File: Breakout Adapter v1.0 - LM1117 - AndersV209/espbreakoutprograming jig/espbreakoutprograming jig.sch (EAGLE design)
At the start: 15 parts, among them X1 MINI-USB_SHIELD4P-85-32004-00X

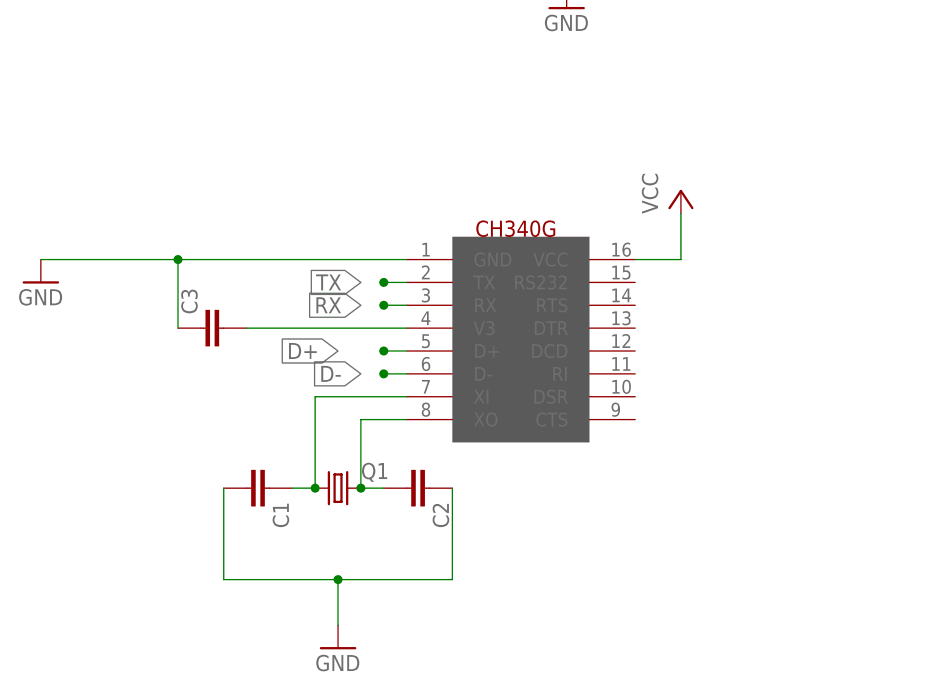
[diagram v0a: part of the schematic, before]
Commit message: update to programming jig
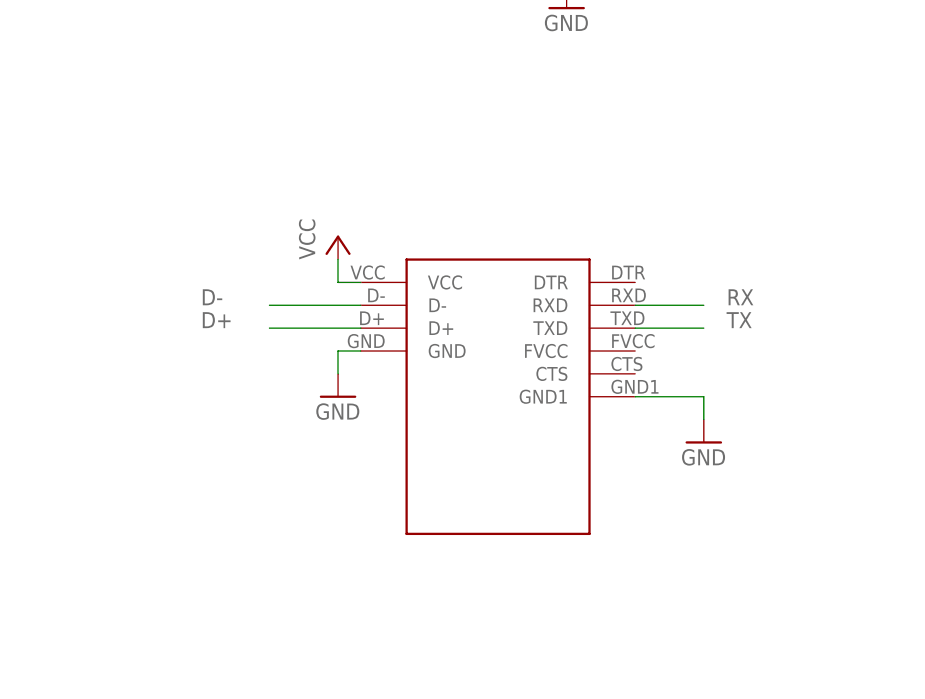
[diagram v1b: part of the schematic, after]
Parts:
- removed C1, C2, C3: (no value), rcl:C-EUC0805K
- removed Q1: (no value), adafruit:CRYSTALHC49U-V
- U$1: value CH340G -> USB-TTL; device usb-serial:CH340G -> mylib:USB-TTL
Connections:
- removed net N$1: C1.1, Q1.1, U$1.XI
- removed net N$2: C2.2, Q1.2, U$1.XO
- removed net N$3: C3.2, U$1.V3
- net GND: now also U$1.GND1; no longer C1.2, C2.1, C3.1
- net RX: now also U$1.RXD; no longer U$1.RX
- net TX: now also U$1.TXD; no longer U$1.TX
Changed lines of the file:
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@@
 </classes>
 <parts>
-<part name="U$1" library="usb-serial" deviceset="CH340G" device=""/>
 <part name="X1" library="con-cypressindustries" deviceset="MINI-USB_SHIELD4P-" device="85-32004-00X"/>
 <part name="U$2" library="mylib" deviceset="ESP12EBREAKOUT" device=""/>
@@
 <part name="P+3" library="supply1" deviceset="VCC" device=""/>
 <part name="POWER" library="mylib" deviceset="TOGGLE_SWITCH" device=""/>
-<part name="C1" library="rcl" deviceset="C-EU" device="C0805K"/>
-<part name="C2" library="rcl" deviceset="C-EU" device="C0805K"/>
-<part name="Q1" library="adafruit" deviceset="CRYSTAL" device="HC49U-V"/>
-<part name="GND4" library="supply1" deviceset="GND" device=""/>
 <part name="R1" library="rcl" deviceset="R-EU_" device="0207/10"/>
 <part name="LED1" library="adafruit" deviceset="LED" device="5MM"/>
@@
 <part name="GND7" library="supply1" deviceset="GND" device=""/>
 <part name="P+4" library="supply1" deviceset="VCC" device=""/>
-<part name="C3" library="rcl" deviceset="C-EU" device="C0805K"/>
 <part name="JP1" library="pinhead" deviceset="PINHD-1X13" device=""/>
 <part name="JP2" library="pinhead" deviceset="PINHD-1X13" device=""/>
+<part name="U$1" library="mylib" deviceset="USB-TTL" device=""/>
+<part name="GND4" library="supply1" deviceset="GND" device=""/>
 </parts>
 <sheets>
@@
 </plain>
 <instances>
-<instance part="U$1" gate="G$1" x="60.96" y="43.18"/>
 <instance part="X1" gate="G$1" x="50.8" y="96.52"/>
 <instance part="U$2" gate="G$1" x="121.92" y="58.42"/>
 <instance part="GND1" gate="1" x="99.06" y="60.96"/>
 <instance part="GND2" gate="1" x="43.18" y="88.9"/>
-<instance part="GND3" gate="1" x="-15.24" y="58.42"/>
-<instance part="P+1" gate="VCC" x="55.88" y="68.58"/>
+<instance part="GND3" gate="1" x="17.78" y="45.72"/>
+<instance part="P+1" gate="VCC" x="17.78" y="63.5"/>
 <instance part="P+2" gate="VCC" x="43.18" y="106.68"/>
 <instance part="P+3" gate="VCC" x="81.28" y="127"/>
 <instance part="POWER" gate="G$1" x="93.98" y="114.3"/>
-<instance part="C1" gate="G$1" x="10.16" y="35.56" rot="R270"/>
-<instance part="C2" gate="G$1" x="27.94" y="35.56" rot="R270"/>
-<instance part="Q1" gate="G$1" x="17.78" y="35.56"/>
-<instance part="GND4" gate="1" x="17.78" y="17.78"/>
 <instance part="R1" gate="G$1" x="81.28" y="114.3" rot="R90"/>
 <instance part="LED1" gate="G$1" x="111.76" y="106.68" rot="R90"/>
@@
 <instance part="GND7" gate="1" x="144.78" y="116.84"/>
 <instance part="P+4" gate="VCC" x="132.08" y="114.3"/>
-<instance part="C3" gate="G$1" x="2.54" y="53.34" rot="R90"/>
 <instance part="JP1" gate="A" x="208.28" y="68.58"/>
 <instance part="JP2" gate="A" x="238.76" y="68.58"/>
+<instance part="U$1" gate="G$1" x="35.56" y="43.18"/>
+<instance part="GND4" gate="1" x="58.42" y="40.64"/>
 </instances>
 <busses>
@@
 </segment>
 <segment>
-<pinref part="C1" gate="G$1" pin="2"/>
-<wire x1="5.08" y1="35.56" x2="5.08" y2="25.4" width="0.1524" layer="91"/>
-<wire x1="5.08" y1="25.4" x2="17.78" y2="25.4" width="0.1524" layer="91"/>
-<wire x1="17.78" y1="25.4" x2="17.78" y2="20.32" width="0.1524" layer="91"/>
-<pinref part="C2" gate="G$1" pin="1"/>
-<wire x1="30.48" y1="35.56" x2="30.48" y2="25.4" width="0.1524" layer="91"/>
-<wire x1="30.48" y1="25.4" x2="17.78" y2="25.4" width="0.1524" layer="91"/>
-<junction x="17.78" y="25.4"/>
-<pinref part="GND4" gate="1" pin="GND"/>
-</segment>
-<segment>
 <pinref part="LED1" gate="G$1" pin="C"/>
 <pinref part="GND5" gate="1" pin="GND"/>
@@
 </segment>
 <segment>
+<pinref part="GND3" gate="1" pin="GND"/>
+<wire x1="17.78" y1="48.26" x2="17.78" y2="50.8" width="0.1524" layer="91"/>
 <pinref part="U$1" gate="G$1" pin="GND"/>
-<pinref part="GND3" gate="1" pin="GND"/>
-<wire x1="25.4" y1="60.96" x2="0" y2="60.96" width="0.1524" layer="91"/>
-<pinref part="C3" gate="G$1" pin="1"/>
-<wire x1="0" y1="60.96" x2="-15.24" y2="60.96" width="0.1524" layer="91"/>
-<wire x1="0" y1="53.34" x2="0" y2="60.96" width="0.1524" layer="91"/>
-<junction x="0" y="60.96"/>
+<wire x1="17.78" y1="50.8" x2="20.32" y2="50.8" width="0.1524" layer="91"/>
+</segment>
+<segment>
+<pinref part="U$1" gate="G$1" pin="GND1"/>
+<wire x1="50.8" y1="45.72" x2="58.42" y2="45.72" width="0.1524" layer="91"/>
+<pinref part="GND4" gate="1" pin="GND"/>
+<wire x1="58.42" y1="45.72" x2="58.42" y2="43.18" width="0.1524" layer="91"/>
 </segment>
 </net>
@@
 <wire x1="45.72" y1="101.6" x2="43.18" y2="101.6" width="0.1524" layer="91"/>
 <wire x1="43.18" y1="101.6" x2="43.18" y2="104.14" width="0.1524" layer="91"/>
-</segment>
-<segment>
-<pinref part="U$1" gate="G$1" pin="VCC"/>
-<pinref part="P+1" gate="VCC" pin="VCC"/>
-<wire x1="50.8" y1="60.96" x2="55.88" y2="60.96" width="0.1524" layer="91"/>
-<wire x1="55.88" y1="60.96" x2="55.88" y2="66.04" width="0.1524" layer="91"/>
 </segment>
 <segment>
@@
 <wire x1="132.08" y1="109.22" x2="134.62" y2="109.22" width="0.1524" layer="91"/>
 </segment>
+<segment>
+<pinref part="P+1" gate="VCC" pin="VCC"/>
+<wire x1="17.78" y1="60.96" x2="17.78" y2="58.42" width="0.1524" layer="91"/>
+<pinref part="U$1" gate="G$1" pin="VCC"/>
+<wire x1="17.78" y1="58.42" x2="20.32" y2="58.42" width="0.1524" layer="91"/>
+</segment>
 </net>
 <net name="D+" class="0">
-<segment>
-<pinref part="U$1" gate="G$1" pin="D+"/>
-<wire x1="25.4" y1="50.8" x2="22.86" y2="50.8" width="0.1524" layer="91"/>
-<junction x="22.86" y="50.8"/>
-<label x="17.78" y="50.8" size="1.778" layer="95" rot="R180" xref="yes"/>
-</segment>
 <segment>
 <pinref part="X1" gate="G$1" pin="3"/>
@@
 <label x="33.02" y="96.52" size="1.778" layer="95" rot="R180" xref="yes"/>
 </segment>
+<segment>
+<pinref part="U$1" gate="G$1" pin="D+"/>
+<wire x1="20.32" y1="53.34" x2="10.16" y2="53.34" width="0.1524" layer="91"/>
+<label x="2.54" y="53.34" size="1.778" layer="95"/>
+</segment>
 </net>
 <net name="D-" class="0">
-<segment>
-<pinref part="U$1" gate="G$1" pin="D-"/>
-<wire x1="25.4" y1="48.26" x2="22.86" y2="48.26" width="0.1524" layer="91"/>
-<junction x="22.86" y="48.26"/>
-<label x="20.32" y="48.26" size="1.778" layer="95" rot="R180" xref="yes"/>
-</segment>
 <segment>
 <pinref part="X1" gate="G$1" pin="2"/>
@@
 <label x="30.48" y="99.06" size="1.778" layer="95" rot="R180" xref="yes"/>
 </segment>
+<segment>
+<pinref part="U$1" gate="G$1" pin="D-"/>
+<wire x1="20.32" y1="55.88" x2="10.16" y2="55.88" width="0.1524" layer="91"/>
+<label x="2.54" y="55.88" size="1.778" layer="95"/>
+</segment>
 </net>
 <net name="TX" class="0">
-<segment>
-<pinref part="U$1" gate="G$1" pin="TX"/>
-<wire x1="25.4" y1="58.42" x2="22.86" y2="58.42" width="0.1524" layer="91"/>
-<junction x="22.86" y="58.42"/>
-<label x="20.32" y="58.42" size="1.778" layer="95" rot="R180" xref="yes"/>
-</segment>
 <segment>
 <pinref part="U$2" gate="G$1" pin="RX"/>
@@
 <label x="223.52" y="81.28" size="1.778" layer="95" rot="R180"/>
 </segment>
+<segment>
+<pinref part="U$1" gate="G$1" pin="TXD"/>
+<wire x1="50.8" y1="53.34" x2="58.42" y2="53.34" width="0.1524" layer="91"/>
+<label x="60.96" y="53.34" size="1.778" layer="95"/>
+</segment>
 </net>
 <net name="RX" class="0">
-<segment>
-<pinref part="U$1" gate="G$1" pin="RX"/>
-<wire x1="25.4" y1="55.88" x2="22.86" y2="55.88" width="0.1524" layer="91"/>
-<junction x="22.86" y="55.88"/>
-<label x="20.32" y="55.88" size="1.778" layer="95" rot="R180" xref="yes"/>
-</segment>
 <segment>
 <pinref part="U$2" gate="G$1" pin="TX"/>
@@
 <label x="223.52" y="83.82" size="1.778" layer="95" rot="R180"/>
 </segment>
-</net>
-<net name="N$3" class="0">
-<segment>
-<pinref part="U$1" gate="G$1" pin="V3"/>
-<wire x1="25.4" y1="53.34" x2="7.62" y2="53.34" width="0.1524" layer="91"/>
-<pinref part="C3" gate="G$1" pin="2"/>
-</segment>
-</net>
-<net name="N$1" class="0">
-<segment>
-<pinref part="C1" gate="G$1" pin="1"/>
-<pinref part="Q1" gate="G$1" pin="1"/>
-<wire x1="12.7" y1="35.56" x2="15.24" y2="35.56" width="0.1524" layer="91"/>
-<pinref part="U$1" gate="G$1" pin="XI"/>
-<wire x1="25.4" y1="45.72" x2="15.24" y2="45.72" width="0.1524" layer="91"/>
-<wire x1="15.24" y1="45.72" x2="15.24" y2="35.56" width="0.1524" layer="91"/>
-<junction x="15.24" y="35.56"/>
-</segment>
-</net>
-<net name="N$2" class="0">
-<segment>
-<pinref part="Q1" gate="G$1" pin="2"/>
-<pinref part="C2" gate="G$1" pin="2"/>
-<wire x1="20.32" y1="35.56" x2="22.86" y2="35.56" width="0.1524" layer="91"/>
-<wire x1="20.32" y1="35.56" x2="20.32" y2="43.18" width="0.1524" layer="91"/>
-<pinref part="U$1" gate="G$1" pin="XO"/>
-<wire x1="20.32" y1="43.18" x2="25.4" y2="43.18" width="0.1524" layer="91"/>
-<junction x="20.32" y="35.56"/>
-</segment>
-</net>
+<segment>
+<pinref part="U$1" gate="G$1" pin="RXD"/>
+<wire x1="50.8" y1="55.88" x2="58.42" y2="55.88" width="0.1524" layer="91"/>
+<label x="60.96" y="55.88" size="1.778" layer="95"/>
+</segment>
+</net>
